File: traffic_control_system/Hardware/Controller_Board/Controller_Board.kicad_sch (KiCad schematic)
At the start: 0 parts

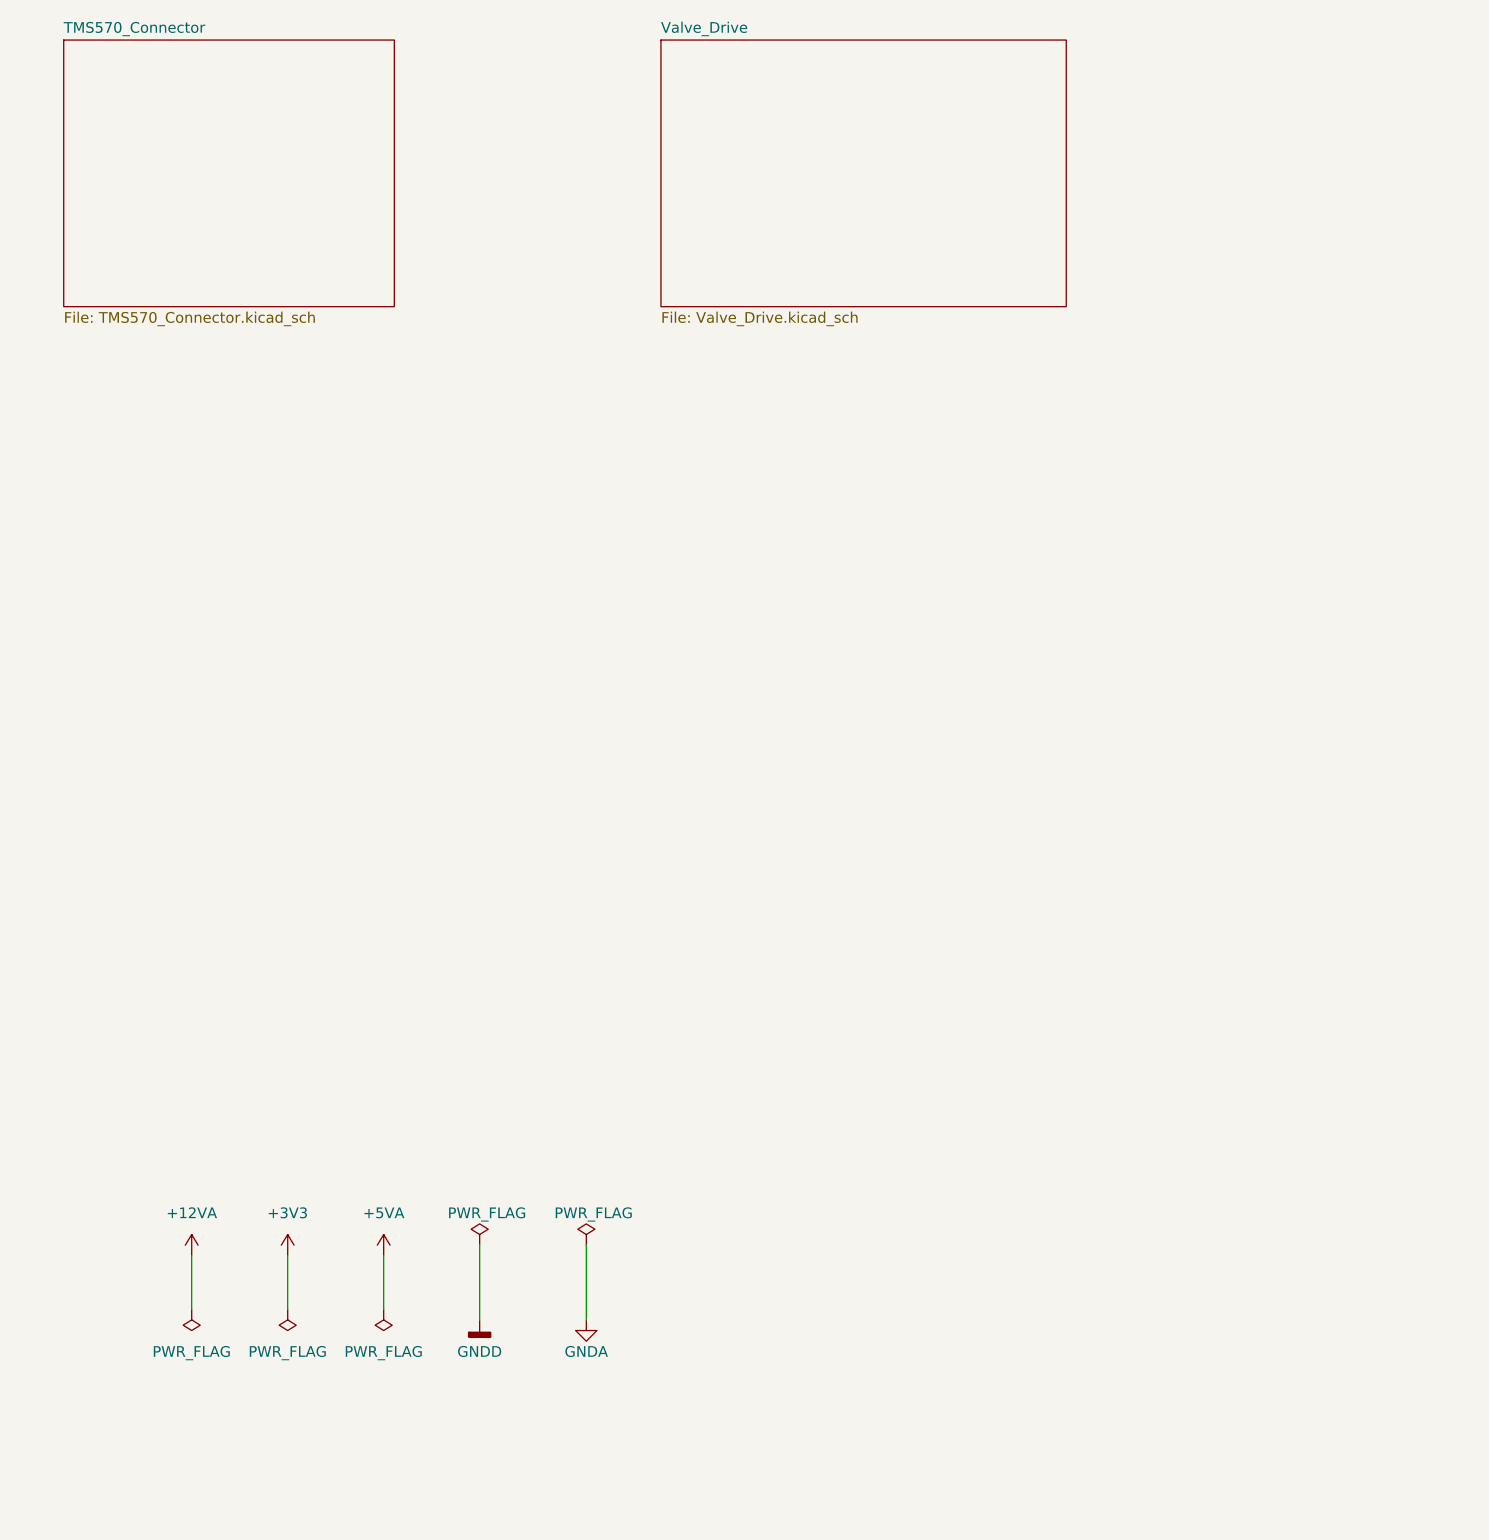
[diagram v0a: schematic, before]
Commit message: issue : 깃 커밋 히스토리 정리를 위한 원본 저장소의 브랜치 분리 작업[TRAFFIC-CONTROL6]
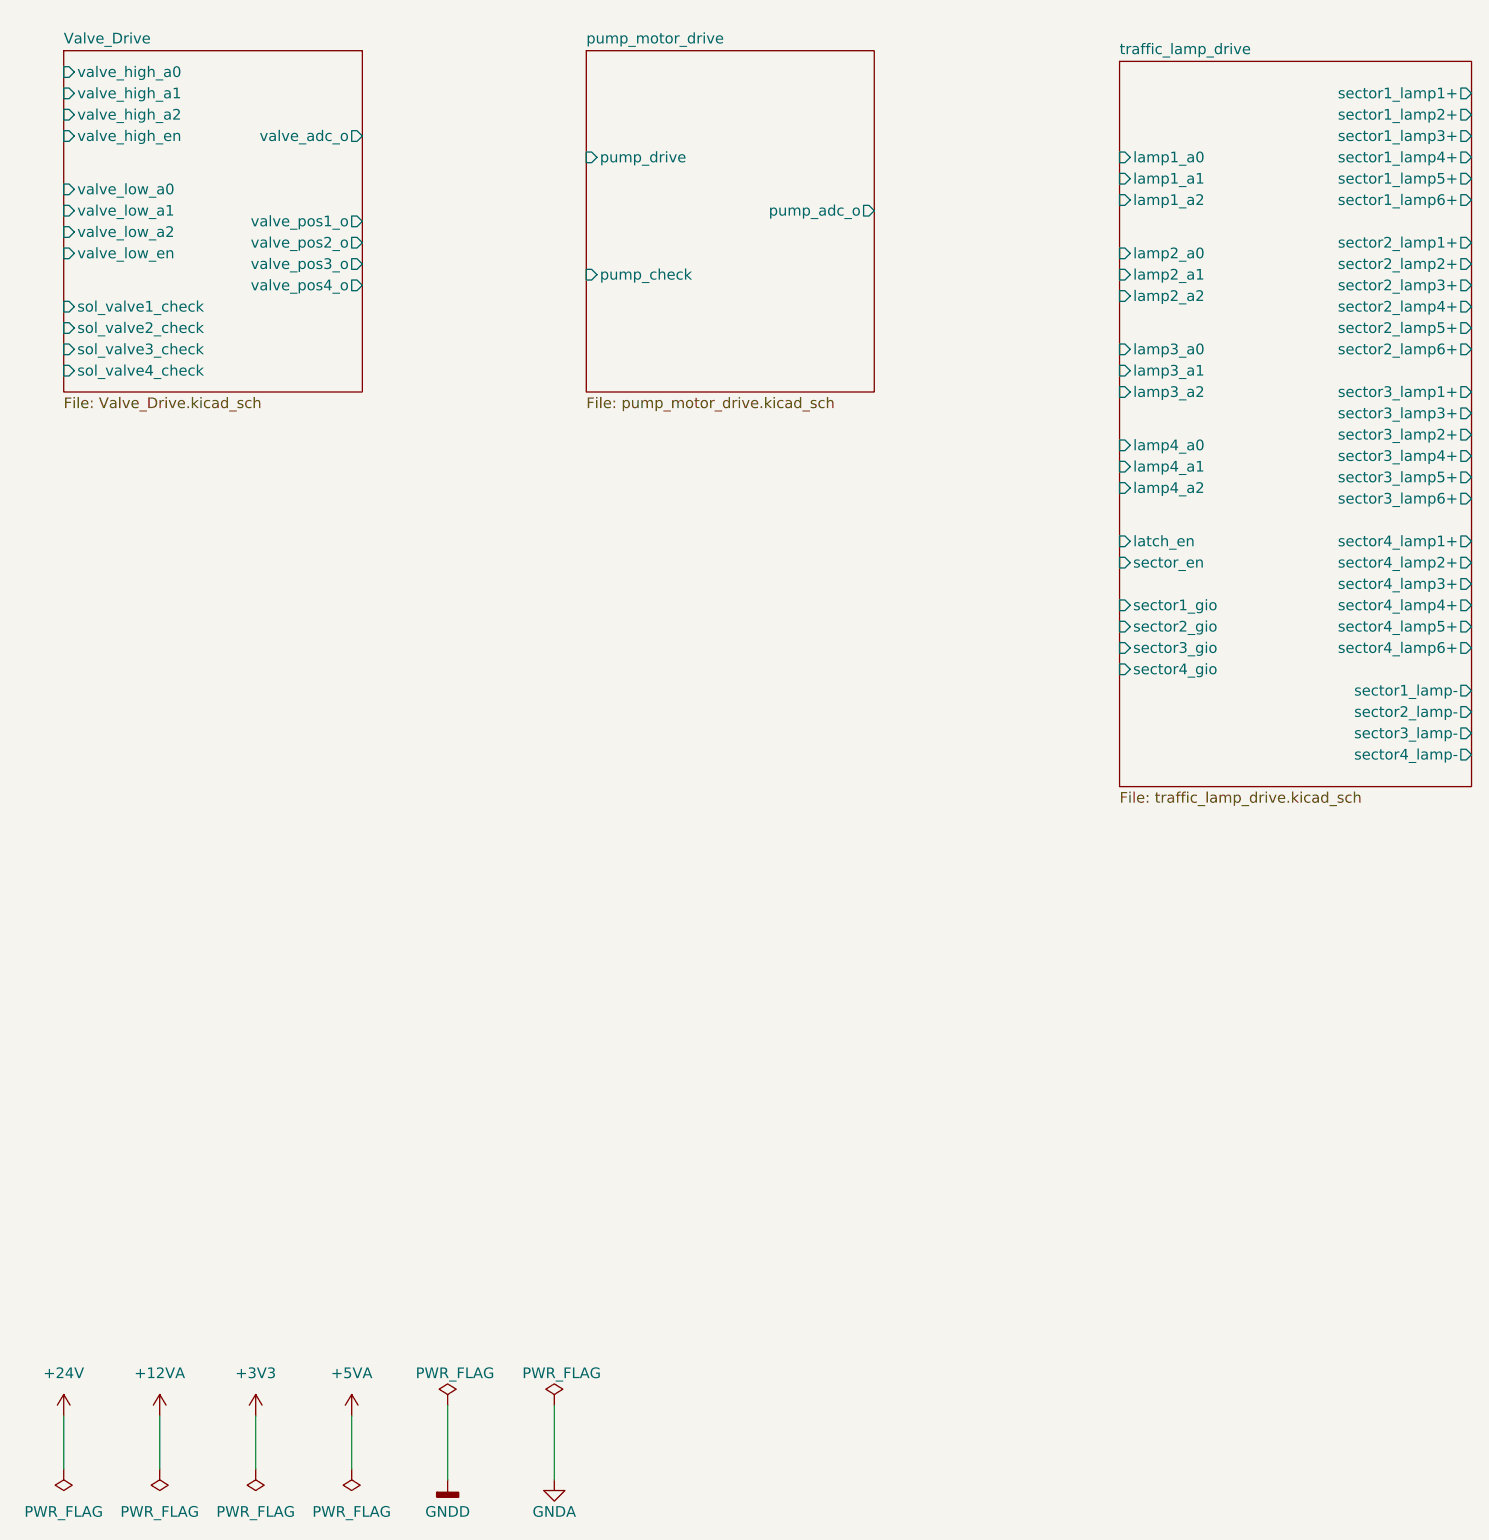
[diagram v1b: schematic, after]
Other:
- removed sheet TMS570_Connector
- added sheet pump_motor_drive (pump_motor_drive.kicad_sch)
- added sheet traffic_lamp_drive (traffic_lamp_drive.kicad_sch)
- sheet Valve_Drive ports: added sol_valve1_check, sol_valve2_check, sol_valve3_check, sol_valve4_check, valve_adc_o, valve_high_a0, valve_high_a1, valve_high_a2, valve_high_en, valve_low_a0, valve_low_a1, valve_low_a2, valve_low_en, valve_pos1_o, valve_pos2_o, valve_pos3_o, valve_pos4_o; removed none
